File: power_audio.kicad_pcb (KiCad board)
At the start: 2 copper layers, 170 x 65 mm, 37 parts, among them J1 Conn_01x03, J2 Conn_01x03, J5 Conn_01x02, Q1 2SC5200, Q10 2SA1943, Q2 2SA1943, Q3 2SC5200, Q4 2SA1943, Q5 2SC5200, Q6 2SA1943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

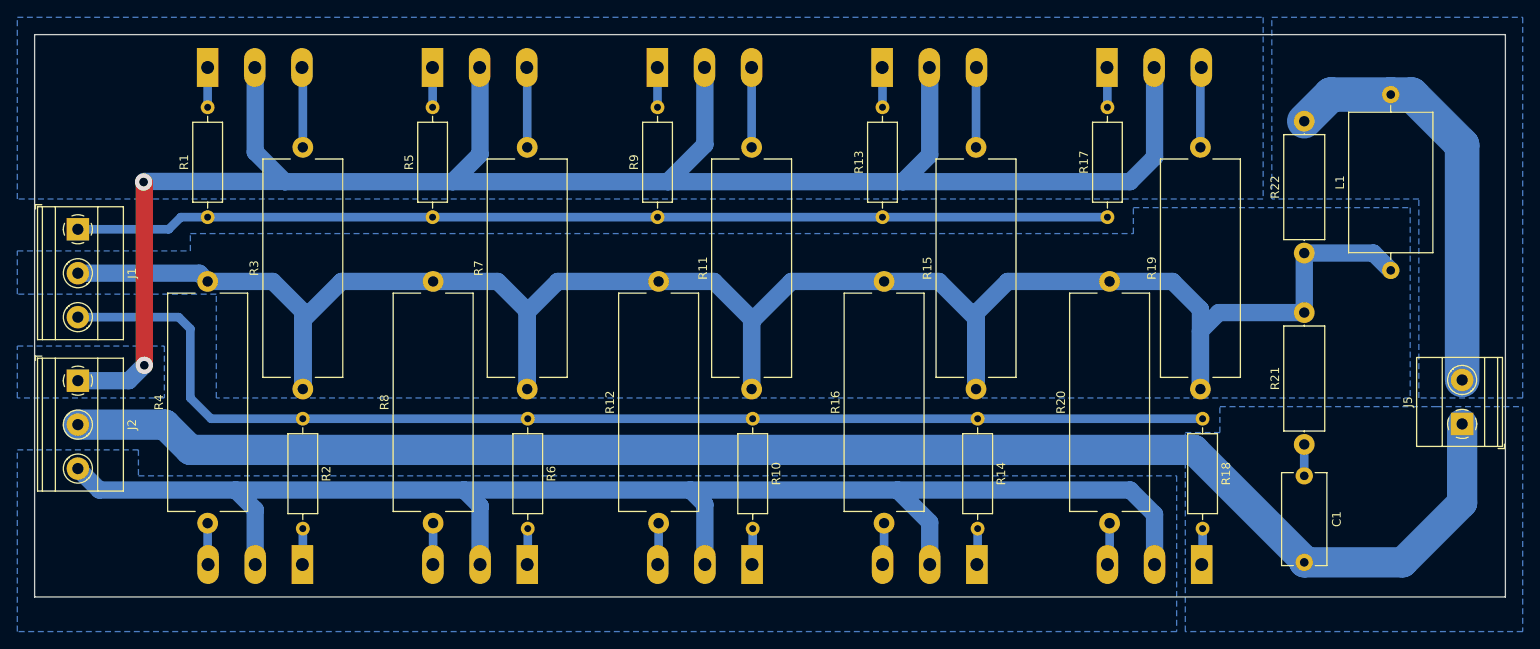
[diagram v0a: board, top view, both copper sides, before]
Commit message: mejorando pistas
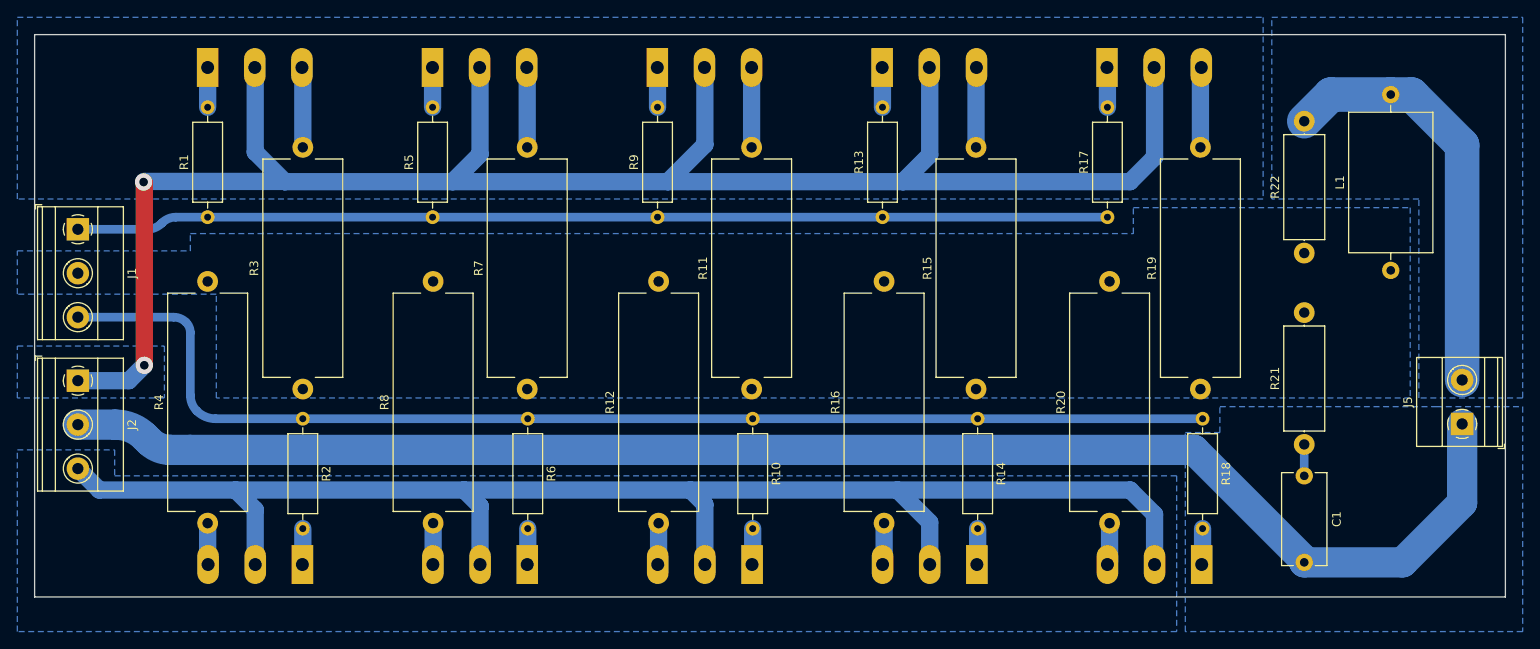
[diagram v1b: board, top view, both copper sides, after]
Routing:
- net /RET: track 258.9 -> 0.00 mm
